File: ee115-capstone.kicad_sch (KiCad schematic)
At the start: 24 parts, among them J2 9V_BATTERY, J5 Conn_01x03_Pin, J6 Conn_02x02_Odd_Even, Q1 PMOS, Q2 NMOS, SW3 SW_Push, U13 LD39150DT33-R

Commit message: added sw
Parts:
- removed R14: 0, Resistor_SMD:R_0805_2012Metric, symbol Device:R
- added SW4: GF-123-0054, footprints:SW2_GF-123-0054_CWI, symbol capstone:GF-123-0054
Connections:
- net +9V: now also SW4.1
- net PWR_IN: now also SW4.2
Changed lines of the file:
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@@
 	(paper "A4")
+	(junction
+		(at 29.21 72.39)
+		(diameter 0)
+		(color 0 0 0 0)
+	)
 	(junction
 		(at 120.015 86.36)
@@
 	)
 	(junction
-		(at 31.75 71.12)
-		(diameter 0)
-		(color 0 0 0 0)
-	)
-	(junction
 		(at 67.31 95.25)
 		(diameter 0)
@@
 	)
 	(junction
-		(at 39.37 72.39)
-		(diameter 0)
-		(color 0 0 0 0)
-	)
-	(junction
 		(at 87.63 74.93)
 		(diameter 0)
@@
 	)
 	(junction
+		(at 44.45 72.39)
+		(diameter 0)
+		(color 0 0 0 0)
+	)
+	(junction
 		(at 33.655 82.55)
 		(diameter 0)
@@
 	)
 	(junction
-		(at 31.75 72.39)
-		(diameter 0)
-		(color 0 0 0 0)
-	)
-	(junction
 		(at 48.26 90.17)
 		(diameter 0)
@@
 	)
 	(junction
-		(at 31.75 82.55)
+		(at 29.21 82.55)
 		(diameter 0)
 		(color 0 0 0 0)
@@
 	(wire
 		(pts
-			(xy 31.75 70.485) (xy 31.75 71.12)
-		)
-		(stroke
-			(width 0)
-			(type default)
-		)
-	)
-	(wire
-		(pts
 			(xy 111.76 101.6) (xy 120.015 101.6)
 		)
@@
 	(wire
 		(pts
-			(xy 31.75 71.12) (xy 31.75 72.39)
+			(xy 29.21 71.12) (xy 29.21 72.39)
 		)
 		(stroke
@@
 	(wire
 		(pts
-			(xy 39.37 72.39) (xy 77.47 72.39)
+			(xy 39.37 72.39) (xy 44.45 72.39)
 		)
 		(stroke
@@
 	(wire
 		(pts
+			(xy 44.45 72.39) (xy 77.47 72.39)
+		)
+		(stroke
+			(width 0)
+			(type default)
+		)
+	)
+	(wire
+		(pts
 			(xy 121.92 82.55) (xy 125.857 82.55)
 		)
@@
 	(wire
 		(pts
-			(xy 31.75 72.39) (xy 31.75 82.55)
-		)
-		(stroke
-			(width 0)
-			(type default)
-		)
-	)
-	(wire
-		(pts
 			(xy 120.015 77.47) (xy 111.76 77.47)
 		)
@@
 	(wire
 		(pts
-			(xy 31.75 82.55) (xy 29.21 82.55)
-		)
-		(stroke
-			(width 0)
-			(type default)
-		)
-	)
-	(wire
-		(pts
 			(xy 87.63 73.66) (xy 92.71 73.66)
 		)
@@
 	(wire
 		(pts
-			(xy 31.75 82.55) (xy 33.655 82.55)
-		)
-		(stroke
-			(width 0)
-			(type default)
-		)
-	)
-	(wire
-		(pts
 			(xy 127 24.13) (xy 134.62 24.13)
 		)
@@
 	(wire
 		(pts
+			(xy 29.21 72.39) (xy 29.21 82.55)
+		)
+		(stroke
+			(width 0)
+			(type default)
+		)
+	)
+	(wire
+		(pts
 			(xy 111.76 73.66) (xy 121.92 73.66)
 		)
@@
 		(pts
 			(xy 43.18 90.17) (xy 48.26 90.17)
+		)
+		(stroke
+			(width 0)
+			(type default)
+		)
+	)
+	(wire
+		(pts
+			(xy 29.21 82.55) (xy 33.655 82.55)
 		)
 		(stroke
@@
 	)
 	(symbol
+		(lib_id "capstone:GF-123-0054")
+		(at 36.83 72.39 0)
+		(unit 1)
+		(exclude_from_sim no)
+		(in_bom yes)
+		(on_board yes)
+		(dnp no)
+		(fields_autoplaced yes)
+		(property "Reference" "SW4"
+			(at 36.83 66.04 0)
+			(effects
+				(font
+					(size 1.524 1.524)
+				)
+			)
+		)
+		(property "Value" "GF-123-0054"
+			(at 36.83 68.58 0)
+			(effects
+				(font
+					(size 1.524 1.524)
+				)
+			)
+		)
+		(property "Footprint" "footprints:SW2_GF-123-0054_CWI"
+			(at 36.83 72.39 0)
+			(effects
+				(font
+					(size 1.27 1.27)
+					(italic yes)
+				)
+				(hide yes)
+			)
+		)
+		(property "Datasheet" "GF-123-0054"
+			(at 36.83 72.39 0)
+			(effects
+				(font
+					(size 1.27 1.27)
+					(italic yes)
+				)
+				(hide yes)
+			)
+		)
+		(property "Description" ""
+			(at 36.83 72.39 0)
+			(effects
+				(font
+					(size 1.27 1.27)
+				)
+				(hide yes)
+			)
+		)
+		(pin "1"
+		)
+		(pin "2"
+		)
+		(instances
+			(project ""
+				(path "/80dfed98-7d85-4c9a-bb85-182165e7352f"
+					(reference "SW4")
+					(unit 1)
+				)
+			)
+		)
+	)
+	(symbol
 		(lib_id "Connector:TestPoint")
 		(at 107.315 30.48 0)
@@
 	(symbol
 		(lib_id "power:+9V")
-		(at 31.75 71.12 0)
+		(at 29.21 71.12 0)
 		(unit 1)
 		(exclude_from_sim no)
@@
 		(fields_autoplaced yes)
 		(property "Reference" "#PWR033"
-			(at 31.75 74.93 0)
+			(at 29.21 74.93 0)
 			(effects
 				(font
@@
 		)
 		(property "Value" "+9V"
-			(at 31.75 66.04 0)
+			(at 29.21 66.04 0)
 			(effects
 				(font
@@
 		)
 		(property "Footprint" ""
-			(at 31.75 71.12 0)
+			(at 29.21 71.12 0)
 			(effects
 				(font
@@
 		)
 		(property "Datasheet" ""
-			(at 31.75 71.12 0)
+			(at 29.21 71.12 0)
 			(effects
 				(font
@@
 		)
 		(property "Description" "Power symbol creates a global label with name \"+9V\""
-			(at 31.75 71.12 0)
+			(at 29.21 71.12 0)
 			(effects
 				(font
@@
 					(unit 1)
 				)
-			)
-		)
-	)
-	(symbol
-		(lib_id "Device:R")
-		(at 35.56 72.39 90)
-		(unit 1)
-		(exclude_from_sim no)
-		(in_bom yes)
-		(on_board yes)
-		(dnp no)
-		(fields_autoplaced yes)
-		(property "Reference" "R14"
-			(at 35.56 66.04 90)
-			(effects
-				(font
-					(size 1.27 1.27)
-				)
-			)
-		)
-		(property "Value" "0"
-			(at 35.56 68.58 90)
-			(effects
-				(font
-					(size 1.27 1.27)
-				)
-			)
-		)
-		(property "Footprint" "Resistor_SMD:R_0805_2012Metric"
-			(at 35.56 74.168 90)
-			(effects
-				(font
-					(size 1.27 1.27)
-				)
-				(hide yes)
-			)
-		)
-		(property "Datasheet" "~"
-			(at 35.56 72.39 0)
-			(effects
-				(font
-					(size 1.27 1.27)
-				)
-				(hide yes)
-			)
-		)
-		(property "Description" "Resistor"
-			(at 35.56 72.39 0)
-			(effects
-				(font
-					(size 1.27 1.27)
-				)
-				(hide yes)
-			)
-		)
-		(pin "1"
-		)
-		(pin "2"
-		)
-		(instances
-			(project "ee115-capstone"
-				(path "/80dfed98-7d85-4c9a-bb85-182165e7352f"
-					(reference "R14")
-					(unit 1)
-				)

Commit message: pcb layout draft
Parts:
- removed J6: Conn_02x02_Odd_Even, Connector_Molex:Molex_Mega-Fit_76829-0004_2x02_P5.70mm_Vertical, symbol Connector_Generic:Conn_02x02_Odd_Even
- added J4: Conn_01x04_Pin, Connector_Molex:Molex_KK-254_AE-6410-04A_1x04_P2.54mm_Vertical, symbol Connector:Conn_01x04_Pin
- C3, C50, C51: footprint Capacitor_SMD:C_0805_2012Metric -> footprints_pretty:0805_cap_nosilk
- R11, R12, R13, R49: footprint Resistor_SMD:R_0805_2012Metric -> footprints_pretty:res_0805_nosilk
- SW4: footprint footprints:SW2_GF-123-0054_CWI -> footprints_pretty:SW2_GF-123-0054_CWI
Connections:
- net GND: now also J4.2 (Pin_2), J4.4 (Pin_4)
- net Thermistor: now also J4.1 (Pin_1)
- net Thermopile: now also J4.3 (Pin_3)

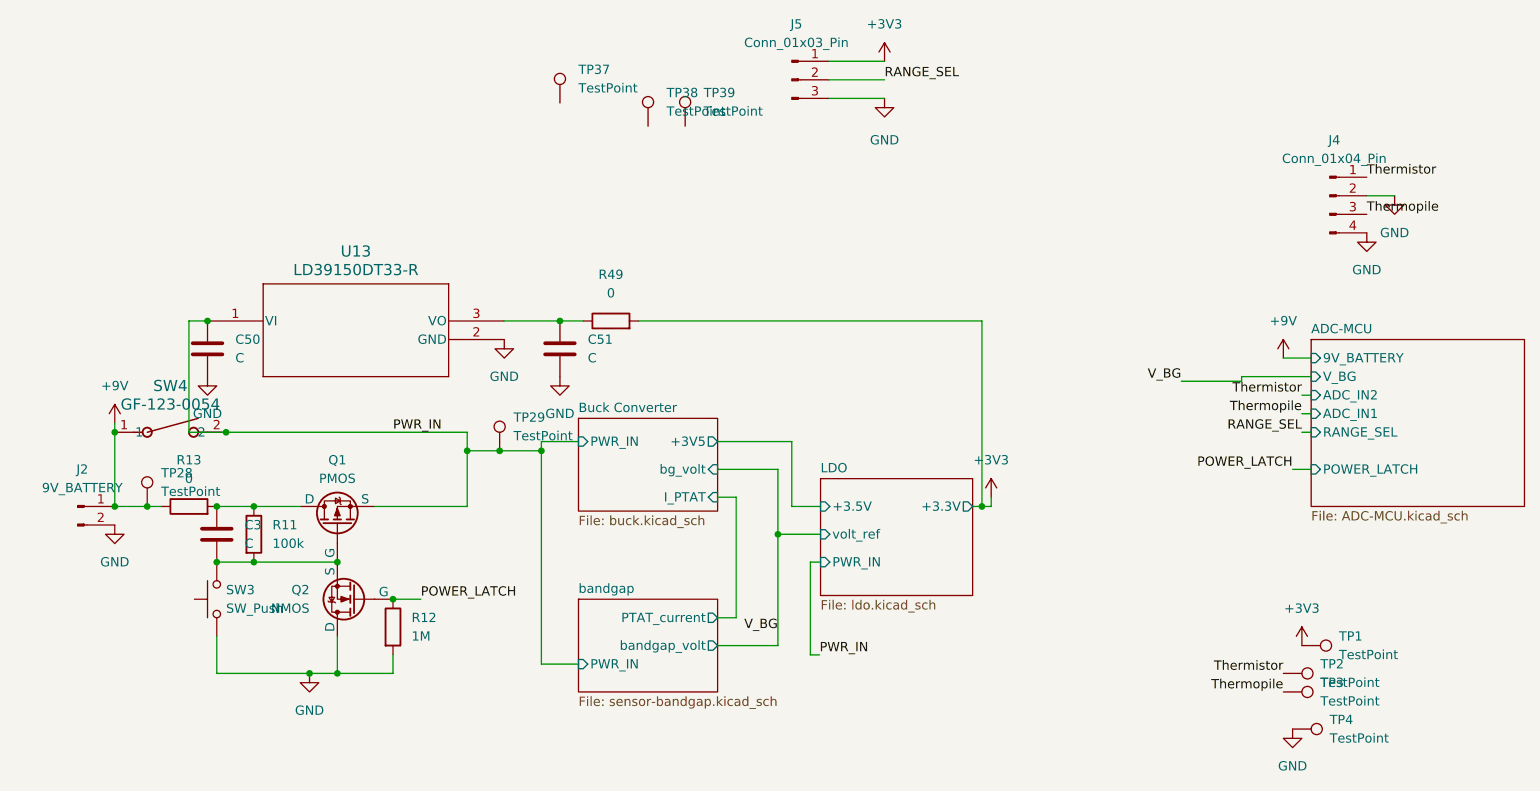
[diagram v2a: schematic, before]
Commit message: fixed drc errors
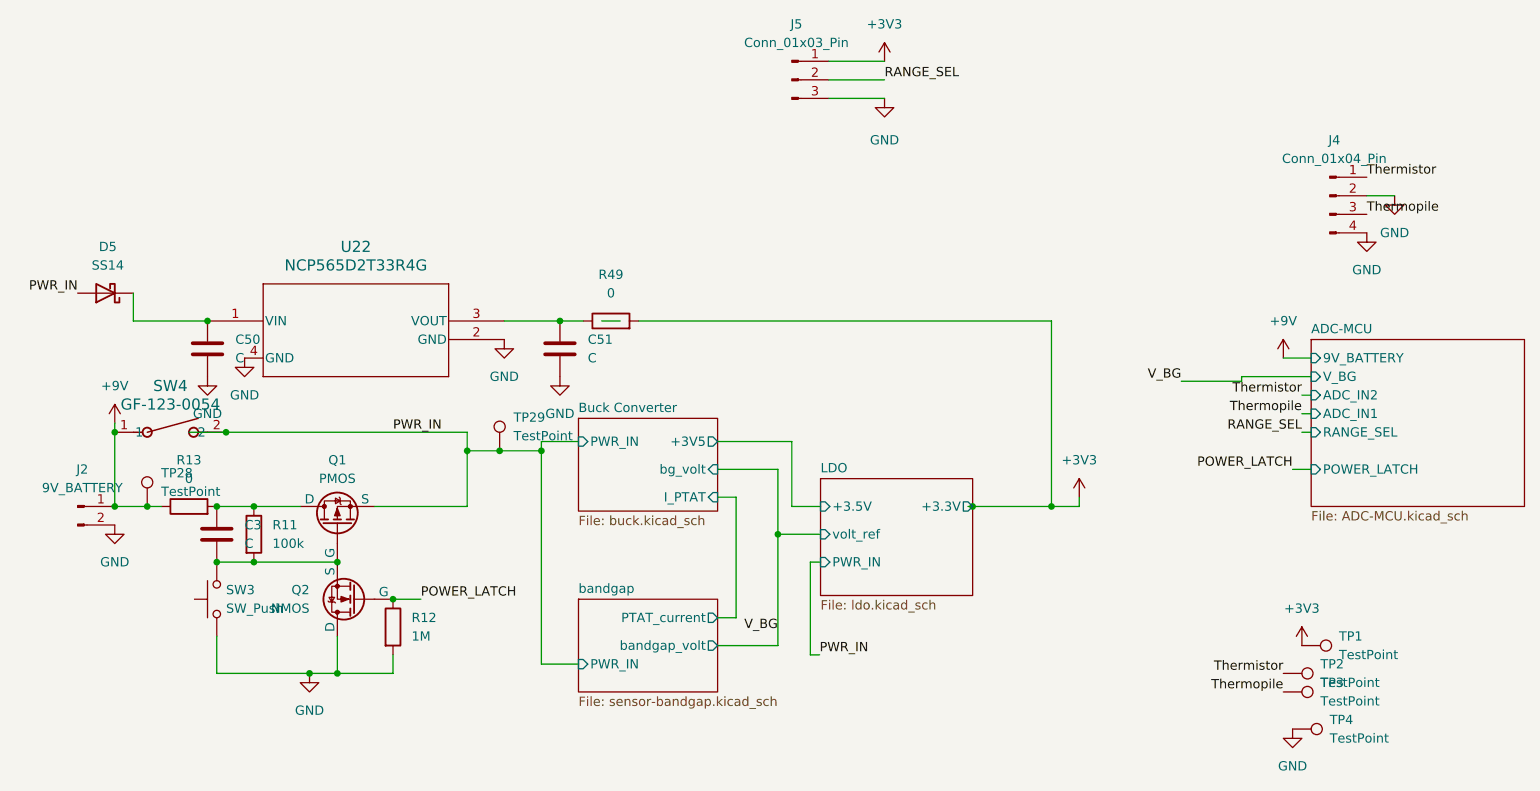
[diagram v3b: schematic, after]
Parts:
- removed TP37, TP38, TP39: TestPoint, MountingHole:MountingHole_3.2mm_M3, symbol Connector:TestPoint
- removed U13: LD39150DT33-R, footprints_pretty:SOT_0DT33-R_STM, symbol LDO1111:LD39150DT33-R
- added D5: SS14, Diode_SMD:D_SMA, symbol Diode:SS14
- added U22: NCP565D2T33R4G, footprints:D2PAK3_ONS, symbol capstone:NCP565D2T33R4G
- SW4: footprint footprints_pretty:SW2_GF-123-0054_CWI -> footprints:SW2_GF-123-0054_CWI
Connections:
- net GND: now also U22.2 (GND), U22.4 (GND)
- net PWR_IN: now also D5.2 (A); no longer C50.1
- net at C51.1, R49.1: now also U22.3 (VOUT)
- new net: C50.1, D5.1 (K), U22.1 (VIN)

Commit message: updated components
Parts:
- renumbered C50 to C101, C51 to C102, D5 to D101, R49 to R101, SW4 to SW101, U22 to U101
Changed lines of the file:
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@@
 		(dnp no)
 		(fields_autoplaced yes)
-		(property "Reference" "D5"
+		(property "Reference" "D101"
 			(at 28.2575 46.99 0)
 			(effects
@@
 			(project "ee115-capstone"
 				(path "/80dfed98-7d85-4c9a-bb85-182165e7352f"
-					(reference "D5")
+					(reference "D101")
 					(unit 1)
 				)
@@
 		(dnp no)
 		(fields_autoplaced yes)
-		(property "Reference" "C51"
+		(property "Reference" "C102"
 			(at 93.98 59.6899 0)
 			(effects
@@
 			(project "ee115-capstone"
 				(path "/80dfed98-7d85-4c9a-bb85-182165e7352f"
-					(reference "C51")
+					(reference "C102")
 					(unit 1)
 				)
@@
 		(dnp no)
 		(fields_autoplaced yes)
-		(property "Reference" "SW4"
+		(property "Reference" "SW101"
 			(at 36.83 66.04 0)
 			(effects
@@
 			(project "ee115-capstone"
 				(path "/80dfed98-7d85-4c9a-bb85-182165e7352f"
-					(reference "SW4")
+					(reference "SW101")
 					(unit 1)
 				)
@@
 		(dnp no)
 		(fields_autoplaced yes)
-		(property "Reference" "U22"
+		(property "Reference" "U101"
 			(at 62.23 46.99 0)
 			(effects
@@
 			(project ""
 				(path "/80dfed98-7d85-4c9a-bb85-182165e7352f"
-					(reference "U22")
+					(reference "U101")
 					(unit 1)
 				)
@@
 		(dnp no)
 		(fields_autoplaced yes)
-		(property "Reference" "R49"
+		(property "Reference" "R101"
 			(at 97.155 50.8 90)
 			(effects
@@
 			(project "ee115-capstone"
 				(path "/80dfed98-7d85-4c9a-bb85-182165e7352f"
-					(reference "R49")
+					(reference "R101")
 					(unit 1)
 				)
@@
 		(dnp no)
 		(fields_autoplaced yes)
-		(property "Reference" "C50"
+		(property "Reference" "C101"
 			(at 45.72 59.6899 0)
 			(effects
@@
 			(project "ee115-capstone"
 				(path "/80dfed98-7d85-4c9a-bb85-182165e7352f"
-					(reference "C50")
-					(unit 1)
-				)
+					(reference "C101")
+					(unit 1)
+				)

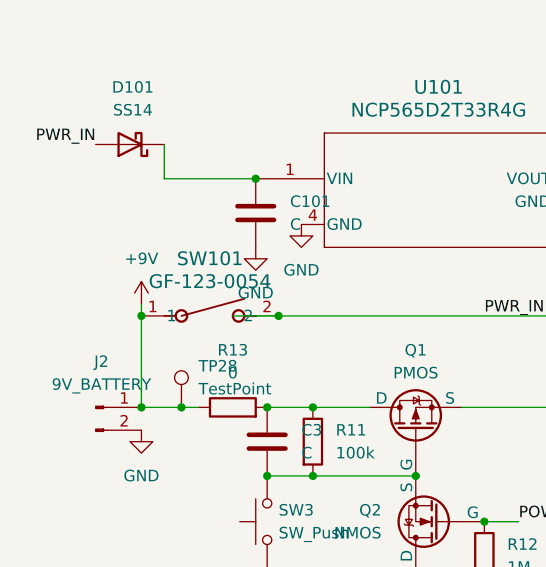
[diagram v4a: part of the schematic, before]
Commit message: fixed battery connection
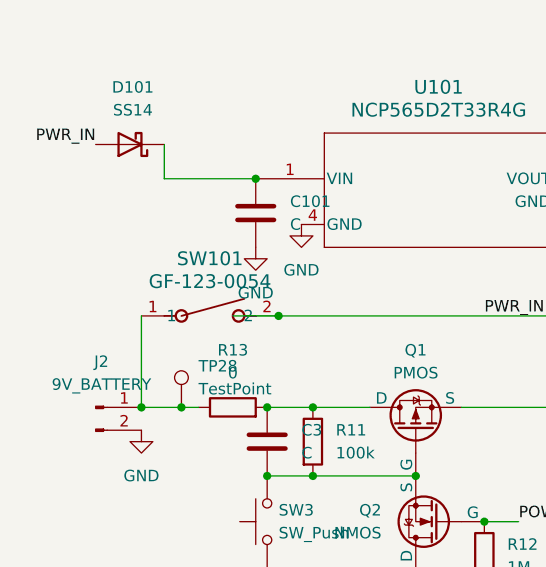
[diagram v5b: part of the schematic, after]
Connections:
- net +9V: no longer J2.1 (Pin_1), R13.1, SW101.1, TP28.1
- new net: J2.1 (Pin_1), R13.1, SW101.1, TP28.1
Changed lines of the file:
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@@
-	)
-	(junction
-		(at 29.21 72.39)
-		(diameter 0)
-		(color 0 0 0 0)
 	)
 	(junction
@@
 		(pts
 			(xy 183.515 65.405) (xy 183.515 64.77)
-		)
-		(stroke
-			(width 0)
-			(type default)
-		)
-	)
-	(wire
-		(pts
-			(xy 29.21 71.12) (xy 29.21 72.39)
 		)
 		(stroke
@@
 					(unit 1)
 				)
-			)
-		)
-	)
-	(symbol
-		(lib_id "power:+9V")
-		(at 29.21 71.12 0)
-		(unit 1)
-		(exclude_from_sim no)
-		(in_bom yes)
-		(on_board yes)
-		(dnp no)
-		(fields_autoplaced yes)
-		(property "Reference" "#PWR033"
-			(at 29.21 74.93 0)
-			(effects
-				(font
-					(size 1.27 1.27)
-				)
-				(hide yes)
-			)
-		)
-		(property "Value" "+9V"
-			(at 29.21 66.04 0)
-			(effects
-				(font
-					(size 1.27 1.27)
-				)
-			)
-		)
-		(property "Footprint" ""
-			(at 29.21 71.12 0)
-			(effects
-				(font
-					(size 1.27 1.27)
-				)
-				(hide yes)
-			)
-		)
-		(property "Datasheet" ""
-			(at 29.21 71.12 0)
-			(effects
-				(font
-					(size 1.27 1.27)
-				)
-				(hide yes)
-			)
-		)
-		(property "Description" "Power symbol creates a global label with name \"+9V\""
-			(at 29.21 71.12 0)
-			(effects
-				(font
-					(size 1.27 1.27)
-				)
-				(hide yes)
-			)
-		)
-		(pin "1"
-		)
-		(instances
-			(project ""
-				(path "/80dfed98-7d85-4c9a-bb85-182165e7352f"
-					(reference "#PWR033")
-					(unit 1)
-				)
